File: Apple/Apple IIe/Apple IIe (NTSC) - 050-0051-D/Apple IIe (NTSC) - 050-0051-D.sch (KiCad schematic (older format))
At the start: 0 parts

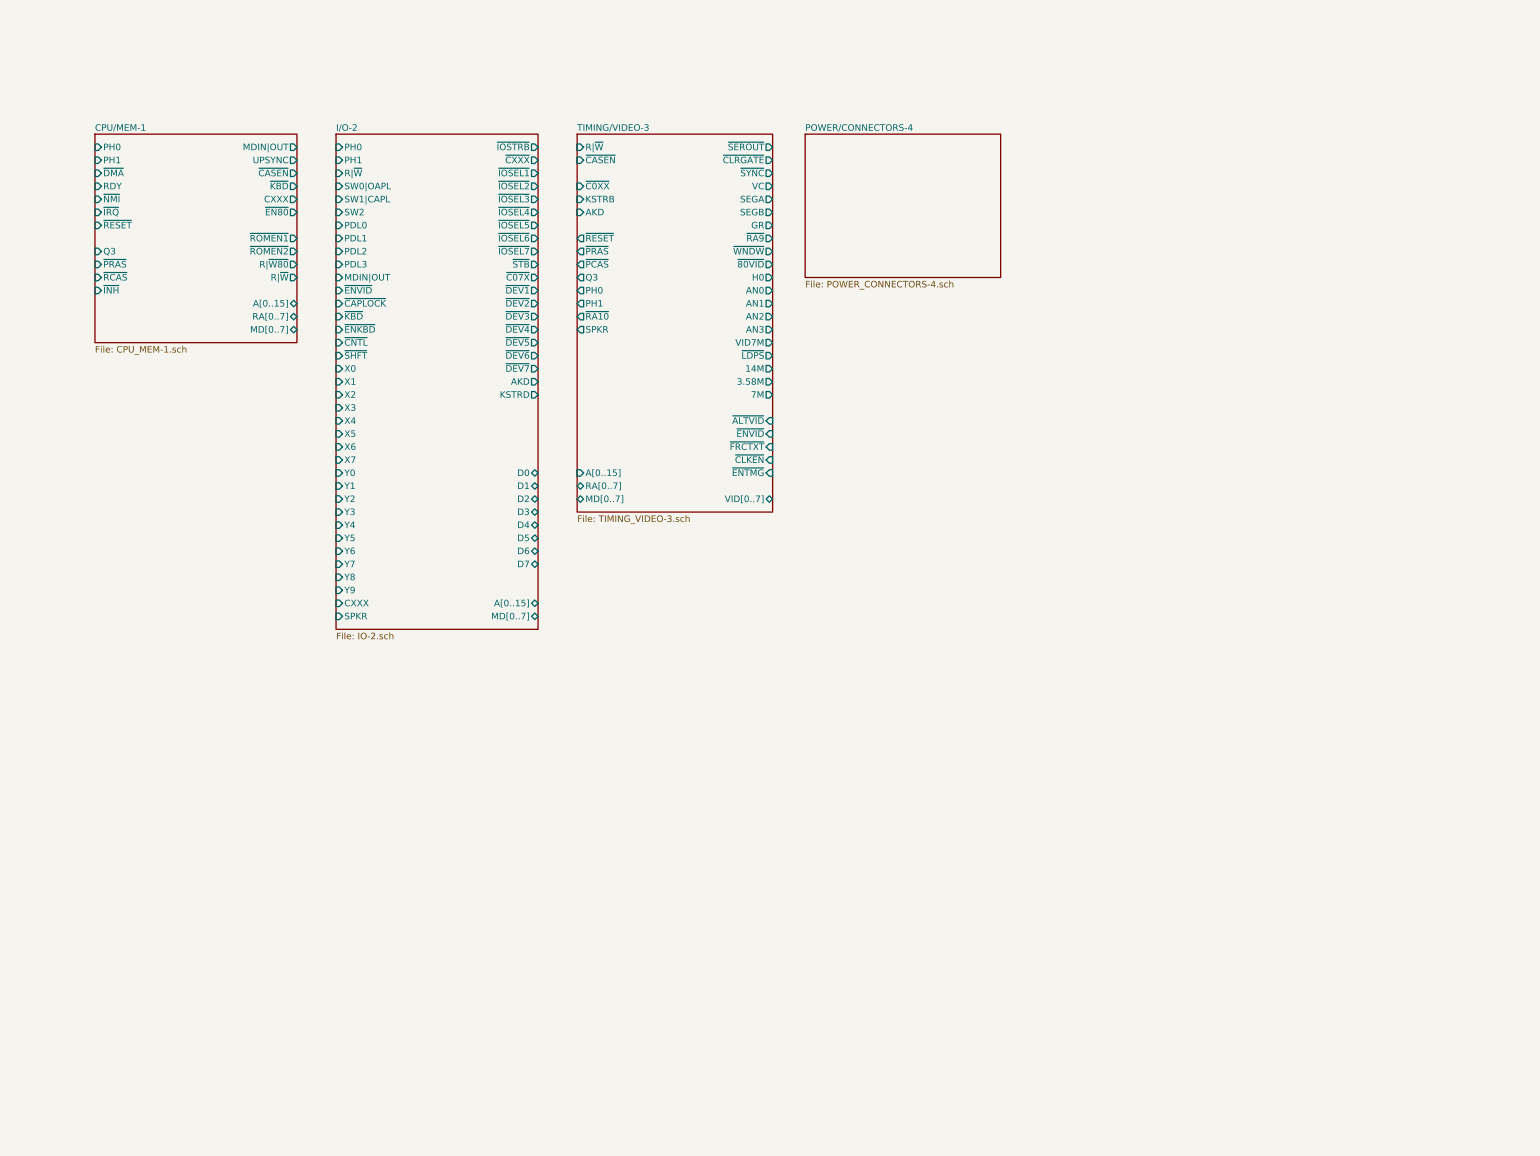
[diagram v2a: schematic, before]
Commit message: Rough top page routing
Probably better if a lot of this is just net labels
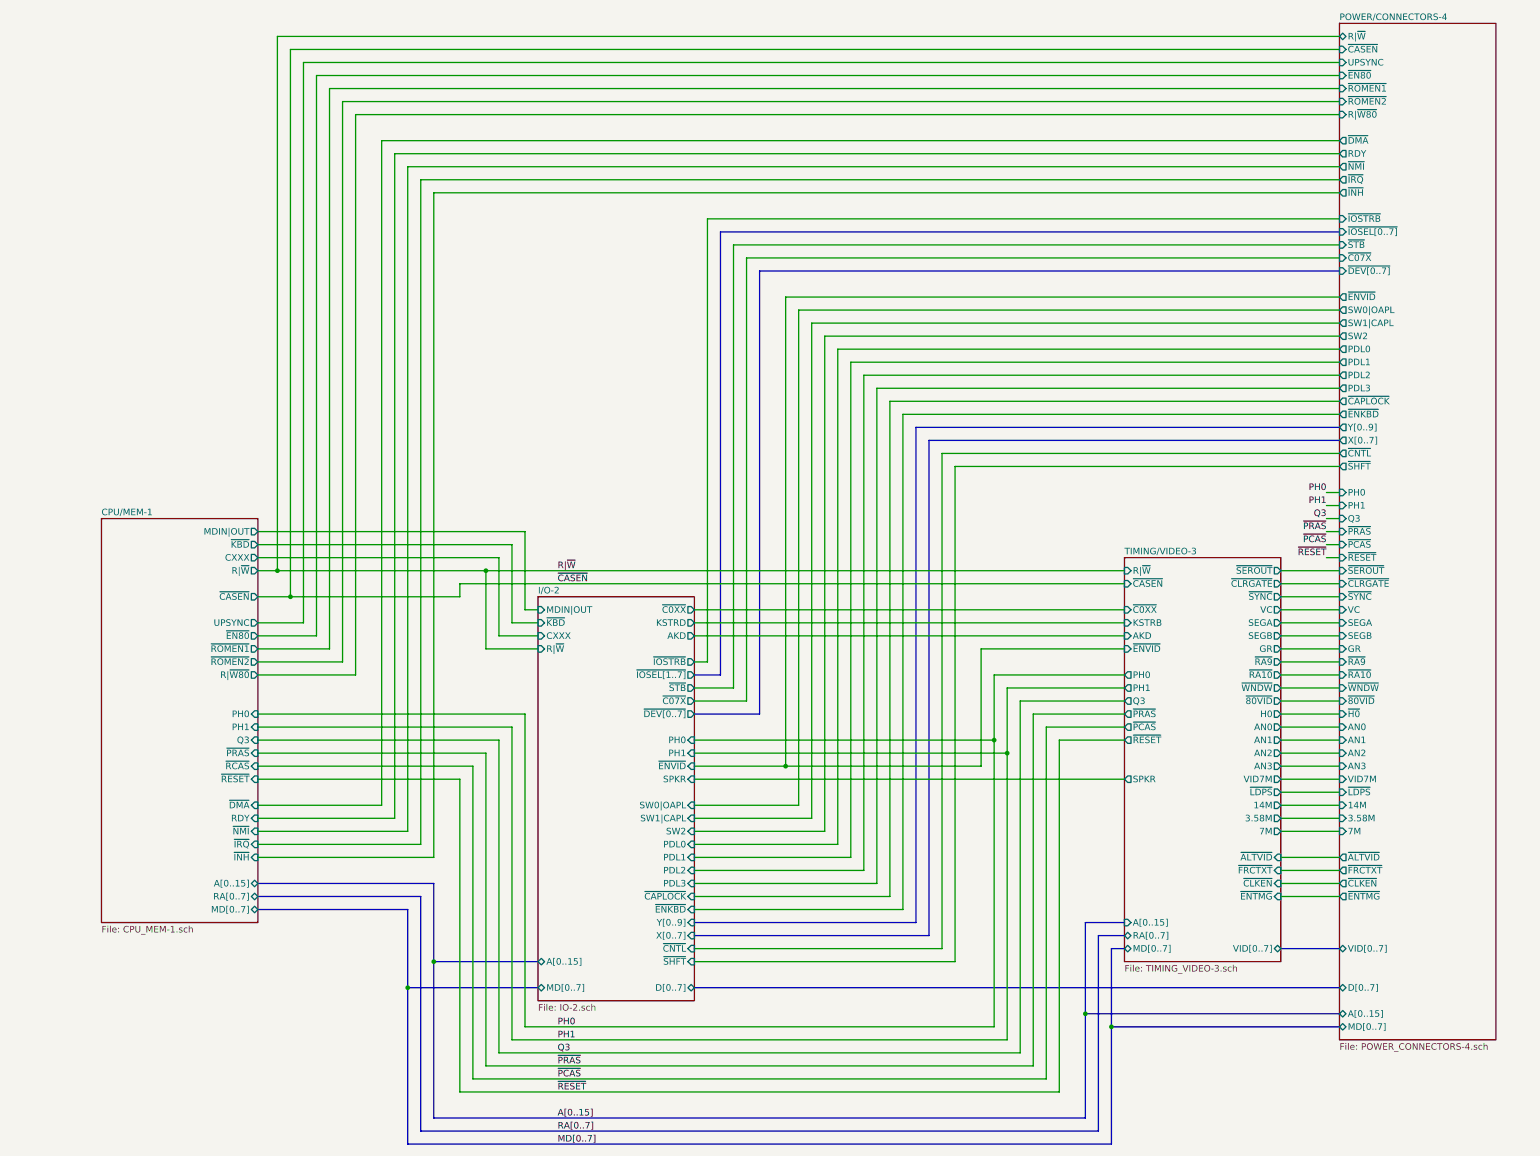
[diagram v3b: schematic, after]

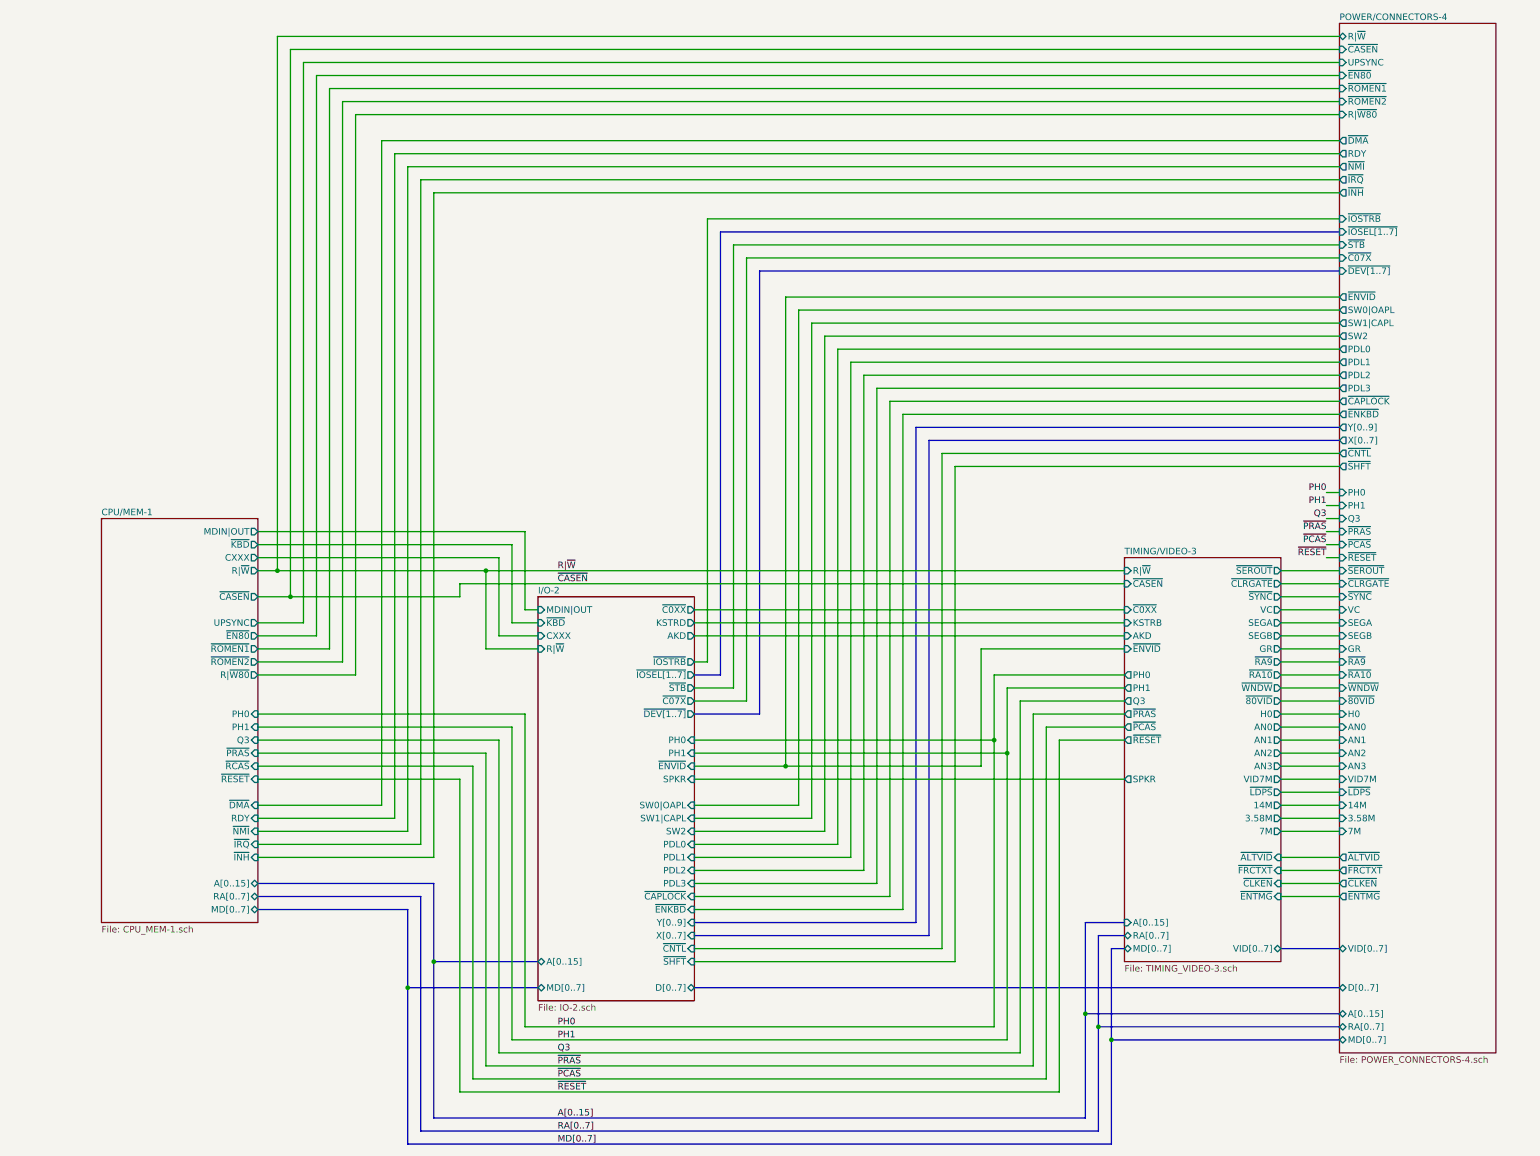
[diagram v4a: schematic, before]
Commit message: Replace | in net labels with _
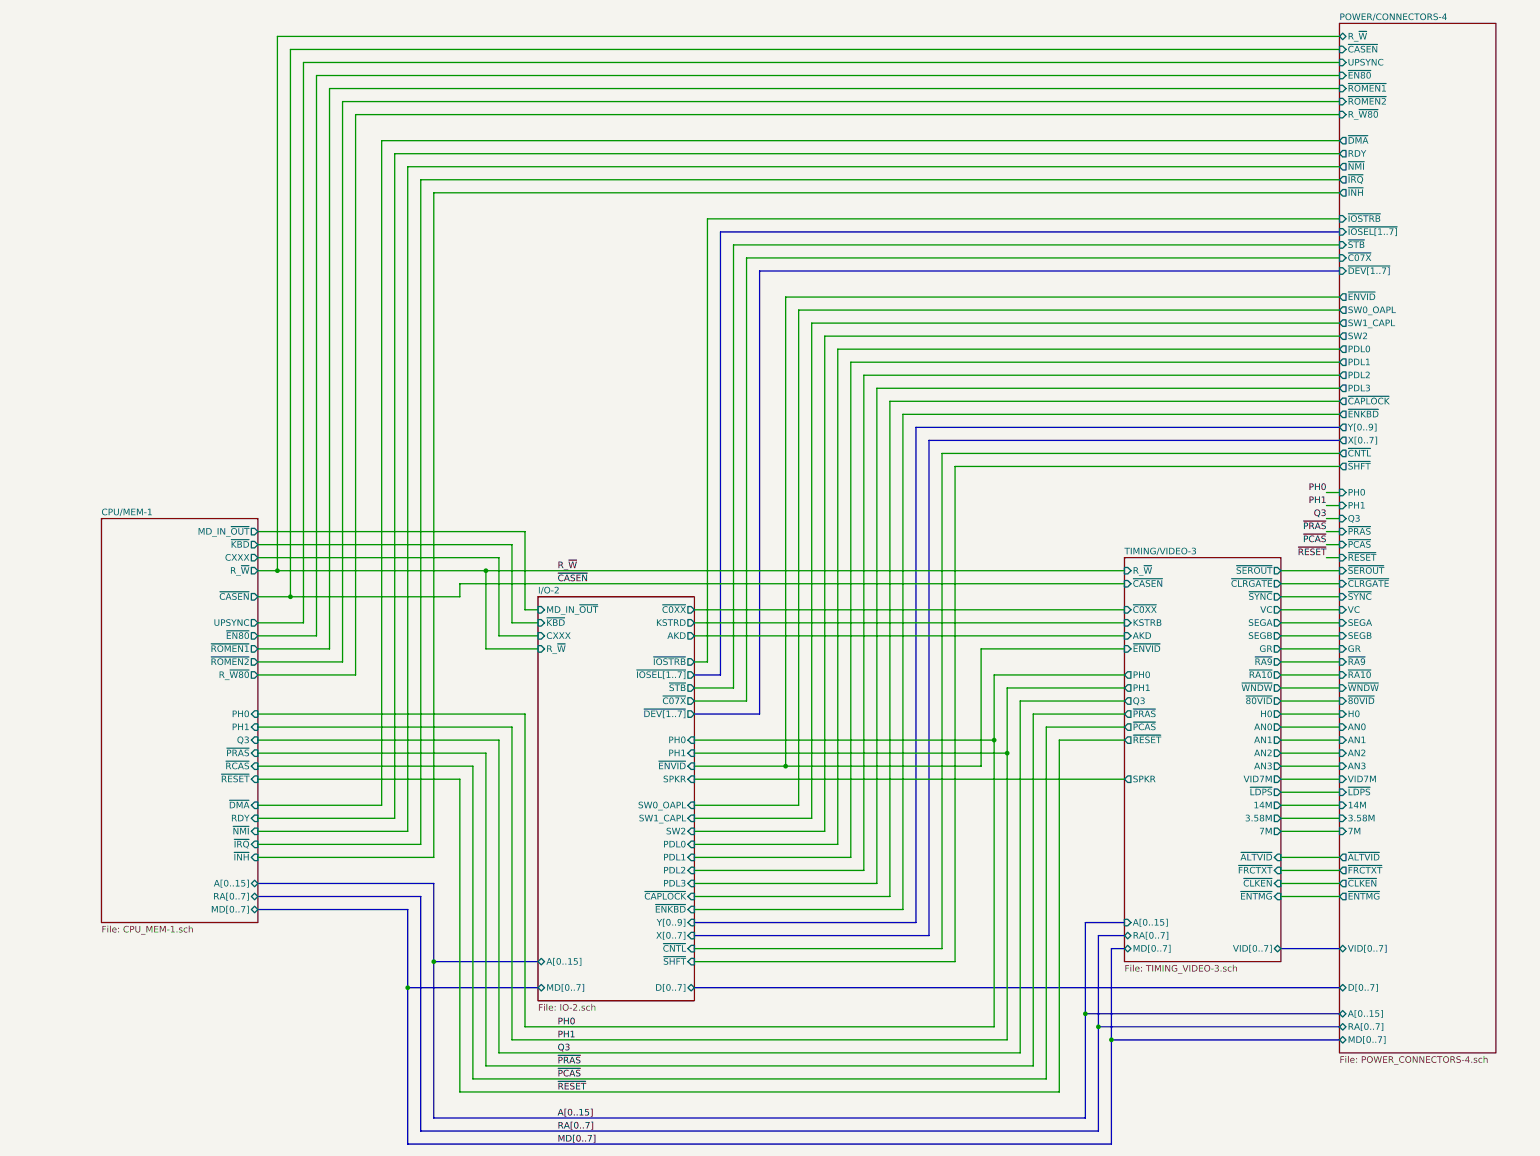
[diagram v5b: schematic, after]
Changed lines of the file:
@@
 F1 "IO-2.sch" 50
 F2 "SW2" I R 7050 7650 50
-F3 "SW1|CAPL" I R 7050 7550 50
-F4 "SW0|OAPL" I R 7050 7450 50
+F3 "SW1_CAPL" I R 7050 7550 50
+F4 "SW0_OAPL" I R 7050 7450 50
 F5 "~IOSTRB" O R 7050 6350 50
 F6 "~STB" O R 7050 6550 50
@@
 F10 "PDL3" I R 7050 8050 50
 F11 "PH0" I R 7050 6950 50
-F12 "R|~W" I L 5850 6250 50
-F13 "MDIN|OUT" I L 5850 5950 50
+F12 "R_~W" I L 5850 6250 50
+F13 "MD_IN_~OUT" I L 5850 5950 50
 F14 "~ENVID" I R 7050 7150 50
 F15 "~CAPLOCK" I R 7050 8150 50
@@
 ~CASEN
 Text Label 6000 5650 0    50   ~ 0
-R|~W
+R_~W
 Wire Bus Line
 	5050 8050 5050 8650
@@
 F11 "~RCAS" I R 3700 7150 50
 F12 "~INH" I R 3700 7850 50
-F13 "R|~W" O R 3700 5650 50
-F14 "R|~W80" O R 3700 6450 50
+F13 "R_~W" O R 3700 5650 50
+F14 "R_~W80" O R 3700 6450 50
 F15 "MD[0..7]" B R 3700 8250 50
 F16 "~ROMEN1" O R 3700 6250 50
@@
 F21 "~CASEN" O R 3700 5850 50
 F22 "UPSYNC" O R 3700 6050 50
-F23 "MDIN|OUT" O R 3700 5350 50
+F23 "MD_IN_~OUT" O R 3700 5350 50
 F24 "A[0..15]" B R 3700 8050 50
 F25 "PH1" I R 3700 6850 50
@@
 F3 "~ENVID" I L 10350 6250 50
 F4 "MD[0..7]" B L 10350 8550 50
-F5 "R|~W" I L 10350 5650 50
+F5 "R_~W" I L 10350 5650 50
 F6 "~C0XX" I L 10350 5950 50
 F7 "KSTRB" I L 10350 6050 50
@@
 F7 "~ROMEN2" I L 12000 2050 50
 F8 "MD[0..7]" B L 12000 9250 50
-F9 "R|~W80" I L 12000 2150 50
-F10 "R|~W" B L 12000 1550 50
+F9 "R_~W80" I L 12000 2150 50
+F10 "R_~W" B L 12000 1550 50
 F11 "~IOSTRB" I L 12000 2950 50
 F12 "~IOSEL[1..7]" I L 12000 3050 50
@@
 F52 "~IRQ" O L 12000 2650 50
 F53 "~INH" O L 12000 2750 50
-F54 "SW0|OAPL" O L 12000 3650 50
-F55 "SW1|CAPL" O L 12000 3750 50
+F54 "SW0_OAPL" O L 12000 3650 50
+F55 "SW1_CAPL" O L 12000 3750 50
 F56 "SW2" O L 12000 3850 50
 F57 "PDL0" O L 12000 3950 50
